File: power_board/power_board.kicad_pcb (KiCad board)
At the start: 2 copper layers, 62 parts, among them J1 Conn_01x02_Female, J10 Conn_01x01_Male, J11 Conn_01x01_Male, J12 Conn_01x01_Male, J13 Conn_01x04_Female, J2 Conn_01x02_Female, J3 Conn_01x02_Female, J4 Conn_01x02_Female, J5 Conn_01x02_Female, J6 Conn_01x01_Male, J7 Conn_01x01_Male, J8 Screw_Terminal_01x02, J9 Conn_01x01_Male, Q1 2N3904, Q2 2N3906, Q3 2N3904, SW1 SW_Push, U1 ACS758xCB-050B-PFF, U2 ACS758xCB-050B-PFF, U3 MCP2515-EST, U4 MAX31855KASA, U5 MCP2551-I-SN, U6 LM5166X, U7 ATmega328P-AU, Y1 16Mhz, Y2 16Mhz

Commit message: finishing touches
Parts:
- removed C11, C12: 560pF, Capacitor_SMD:C_0603_1608Metric
- removed C6: 10nF, Capacitor_SMD:C_0603_1608Metric
- removed L1, L2: 470ohm, Inductor_SMD:L_0603_1608Metric
- removed R10, R11: 100, Resistor_SMD:R_0603_1608Metric
- removed R6: 4.7k, Resistor_SMD:R_0603_1608Metric
- added J14: M7, TerminalBlock:TerminalBlock_bornier-2_P5.08mm, F.Cu at (81.7, 99.3)
- added J15: FAN, TerminalBlock:TerminalBlock_bornier-2_P5.08mm, F.Cu at (81.7, 107.3)
- added Q4: Q_NMOS_DGS, Package_TO_SOT_SMD:TO-263-2, F.Cu at (70.6, 100.9)
- J1: value Conn_01x02_Female -> PROG; footprint Connector_JST:JST_GH_BM02B-GHS-TBT_1x02-1MP_P1.25mm_Vertical -> Connector_PinHeader_2.54mm:PinHeader_1x05_P2.54mm_Vertical
- J10: value Conn_01x01_Male -> M4; footprint Connector:Banana_Jack_1Pin -> TerminalBlock:TerminalBlock_bornier-2_P5.08mm
- J11: value Conn_01x01_Male -> MainBoard; footprint Connector:Banana_Jack_1Pin -> TerminalBlock:TerminalBlock_bornier-2_P5.08mm
- J12: value Conn_01x01_Male -> M5; footprint Connector:Banana_Jack_1Pin -> TerminalBlock:TerminalBlock_bornier-2_P5.08mm
- J13: value Conn_01x04_Female -> M6; footprint Connector_PinHeader_2.54mm:PinHeader_1x04_P2.54mm_Horizontal -> TerminalBlock:TerminalBlock_bornier-2_P5.08mm
- J2: value Conn_01x02_Female -> M1; footprint Connector_JST:JST_GH_BM02B-GHS-TBT_1x02-1MP_P1.25mm_Vertical -> TerminalBlock:TerminalBlock_bornier-2_P5.08mm
- J3: value Conn_01x02_Female -> M2; footprint Connector_JST:JST_GH_BM02B-GHS-TBT_1x02-1MP_P1.25mm_Vertical -> TerminalBlock:TerminalBlock_bornier-2_P5.08mm
- J9: value Conn_01x01_Male -> M3; footprint Connector:Banana_Jack_1Pin -> TerminalBlock:TerminalBlock_bornier-2_P5.08mm
- Q1, Q3: value 2N3904 -> Q_NMOS_DGS; footprint Package_TO_SOT_SMD:SOT-23 -> Package_TO_SOT_SMD:TO-263-2
- Q2: value 2N3906 -> Q_NMOS_DGS; footprint Package_TO_SOT_SMD:SOT-23 -> Package_TO_SOT_SMD:TO-263-2
- R12: value R_US -> 0
- R2: value 1k -> 10k
- R3: value 27k -> 10k
- R4: value 4.7k -> 10k
- R5: value 1k -> 1.1k
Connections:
- net SYSTEM_SHUTOFF renamed Net-(U7-Pad11)
- J1 pad 1: GNDREF -> +5V
- J1 pad 2: PROBE -> RESET
- J10 pad 1: GNDREF -> +12V
- J11 pad 1: +12VA -> +5V
- J12 pad 1: GNDREF -> +12VA
- J13 pad 1: +5V -> +12VA
- J13 pad 2: TX -> GNDREF
- J2 pad 1: GNDREF -> +12V
- J2 pad 2: PROBE -> GNDREF
- J3 pad 1: GNDREF -> +12V
- J3 pad 2: PROBE -> GNDREF
- J4 pad 2: PROBE -> LEAK_DETECTED
- J5 pad 2: PROBE -> LEAK_DETECTED
- Q1 pad 1: GNDREF -> Net-(Q1-Pad1)
- Q1 pad 2: Net-(Q1-Pad2) -> LEAK_DETECTED
- Q1 pad 3: Net-(Q1-Pad3) -> GNDREF
- Q2 pad 1: +5V -> Net-(Q2-Pad1)
- Q2 pad 2: Net-(Q2-Pad2) -> LEAK_DETECTED
- Q2 pad 3: LEAK_DETECTED -> GNDREF
- Q3 pad 1: GNDREF -> Net-(Q1-Pad1)
- Q3 pad 2: Net-(Q3-Pad2) -> LEAK_DETECTED
- Q3 pad 3: Net-(Q1-Pad3) -> GNDREF
- R14 pad 1: RESET -> +5V
- R14 pad 2: +5V -> RESET
- R2 pad 1: Net-(Q2-Pad2) -> +5VA
- R2 pad 2: PROBE -> LEAK_DETECTED
- R3 pad 1: Net-(Q2-Pad2) -> +5VA
- R3 pad 2: +5V -> LEAK_DETECTED
- R4 pad 1: LEAK_DETECTED -> +5VA
- R4 pad 2: Net-(Q1-Pad2) -> +48V
- R5 pad 2: LEAK_DETECTED -> +5VA
- REG1 pad 2: Net-(Q1-Pad3) -> Net-(Q2-Pad1)
- REG1 pad 3: GNDREF -> Net-(Q2-Pad1)
- REG2 pad 2: Net-(Q1-Pad3) -> Net-(Q1-Pad1)
- REG2 pad 3: GNDREF -> Net-(Q1-Pad1)
- U3 pad 11: Net-(U3-Pad11) -> RX1BF
- U3 pad 12: Net-(U3-Pad12) -> RX_INT
- U3 pad 4: Net-(U3-Pad4) -> TX0RTS
- U3 pad 5: Net-(U3-Pad5) -> TX1RTS
- U3 pad 7: Net-(U3-Pad7) -> TX2RTS
- U4 pad 2: Net-(C6-Pad2) -> Net-(J8-Pad2)
- U4 pad 3: Net-(C6-Pad1) -> Net-(J8-Pad1)
- U7 pad 1: Net-(U7-Pad1) -> RX_INT
- U7 pad 25: Net-(U7-Pad25) -> RX1BF
- U7 pad 26: Net-(U7-Pad26) -> TX0RTS
- U7 pad 27: Net-(U7-Pad27) -> TX1RTS
- U7 pad 28: Net-(U7-Pad28) -> TX2RTS

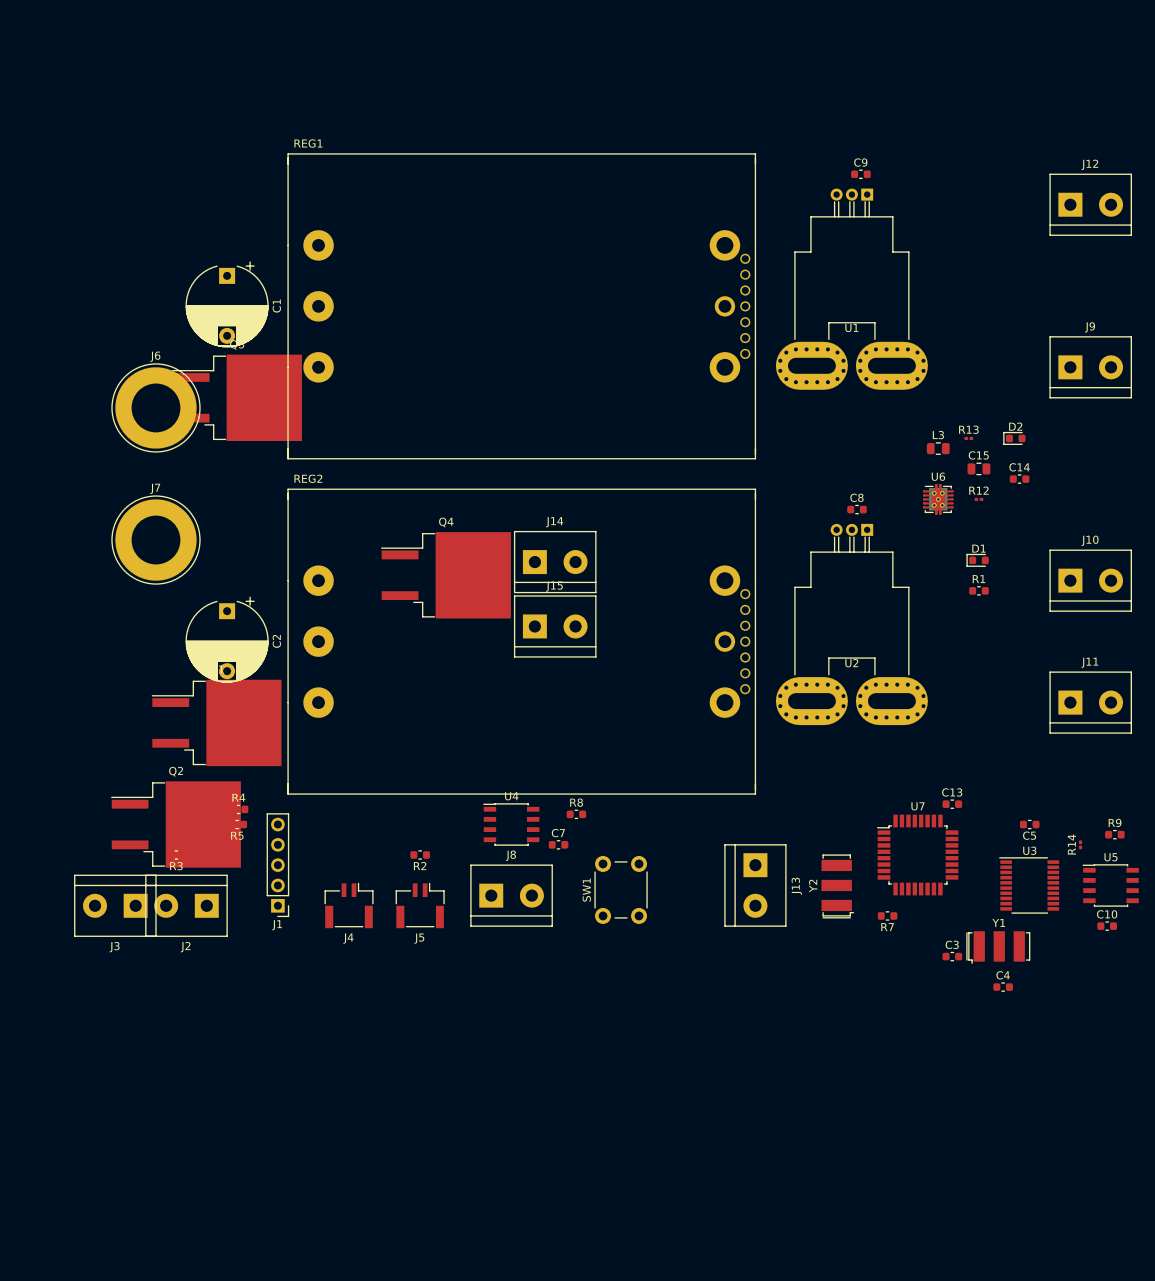
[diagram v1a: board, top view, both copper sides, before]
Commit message: Finished adding power regulator isolation
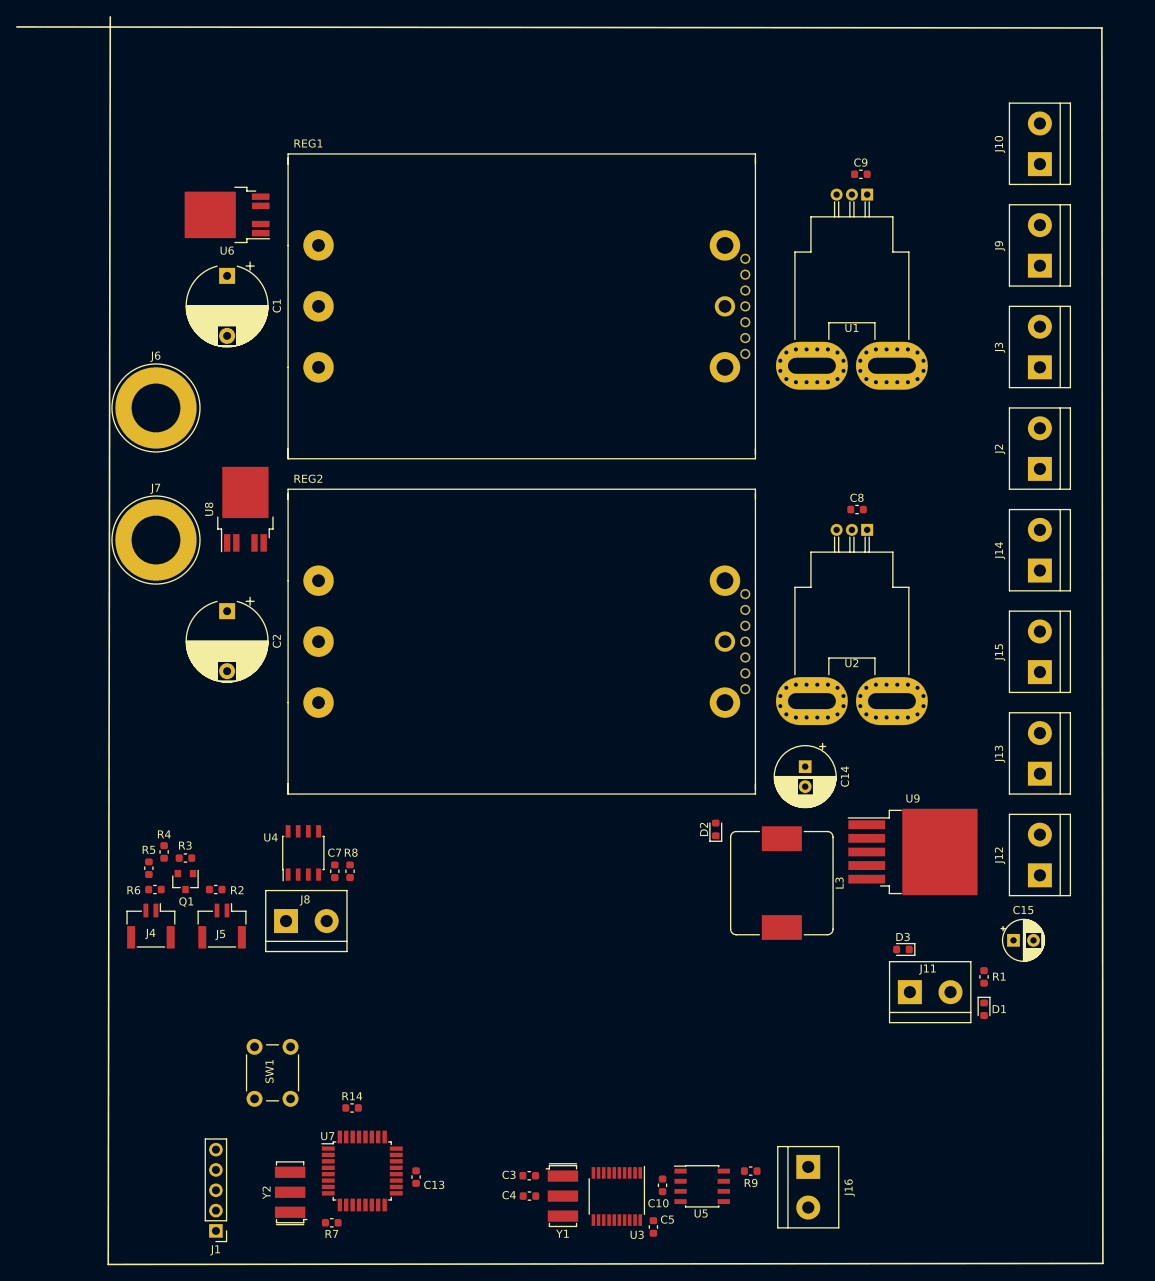
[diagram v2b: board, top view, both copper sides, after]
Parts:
- removed Q2, Q3, Q4: Q_NMOS_DGS, Package_TO_SOT_SMD:TO-263-2
- removed R12: 0, Resistor_SMD:R_0201_0603Metric
- removed R13: 0.5, Resistor_SMD:R_0201_0603Metric
- added D3: --, Diode_SMD:D_0603_1608Metric, F.Cu at (127.7, 147.7)
- added J16: Screw_Terminal_01x02, TerminalBlock:TerminalBlock_bornier-2_P5.08mm, F.Cu at (115.8, 174.9)
- added R6: 10k, Resistor_SMD:R_0603_1608Metric, F.Cu at (34.2, 140.2)
- added U8: BTS6163D, Package_TO_SOT_SMD:TO-252-4, F.Cu at (45.5, 92.7)
- added U9: LM2596S-5, Package_TO_SOT_SMD:TO-263-5_TabPin3, F.Cu at (128.9, 135.5)
- C1, C2: value CP -> 300uF
- C14: value 2.2uF -> 680uF; footprint Capacitor_SMD:C_0603_1608Metric -> Capacitor_THT:CP_Radial_D7.5mm_P2.50mm
- C15: value 47uF -> 220uF; footprint Capacitor_SMD:C_0805_2012Metric -> Capacitor_THT:CP_Radial_D5.0mm_P2.50mm
- D2: value D_Schottky -> 1N5824
- L3: value 150uH -> 33uH; footprint Inductor_SMD:L_0805_2012Metric -> Inductor_SMD:L_Bourns_SRP1245A
- Q1: value Q_NMOS_DGS -> 2N3906; footprint Package_TO_SOT_SMD:TO-263-2 -> Package_TO_SOT_SMD:SOT-23
- R14: footprint Resistor_SMD:R_0201_0603Metric -> Resistor_SMD:R_0603_1608Metric
- R2: value 10k -> 1k
- U6: value LM5166X -> BTS6163D; footprint Package_SON:Texas_S-PVSON-N10_ThermalVias -> Package_TO_SOT_SMD:TO-252-4
- moved J3 131.6 mm to (144.8, 74.9), turned to 90 degrees
- moved J2 117.6 mm to (144.8, 87.6), turned to 90 degrees
- moved R14 96.8 mm to (58.8, 167.5), turned to 0 degrees
- moved U6 95.7 mm to (43.2, 55.9), turned to 180 degrees
- moved J12 83.9 mm to (144.8, 138.4), turned to 90 degrees
- moved C13 81.6 mm to (66.8, 176.1), turned to 90 degrees
- moved U7 79.9 mm to (60.1, 175.4)
- moved R7 79.4 mm to (56.3, 181.9)
- moved Y2 78.4 mm to (51.1, 178.1)
- moved C5 68.9 mm to (96.5, 182.4), turned to 270 degrees
- moved C4 64.7 mm to (81.0, 178.5), turned to 180 degrees
- moved U3 64.6 mm to (91.9, 178.6), turned to 270 degrees
- moved C10 64.3 mm to (97.6, 177.2), turned to 90 degrees
- moved U5 63.5 mm to (102.6, 177.3)
- moved J15 63.4 mm to (144.8, 113.0), turned to 90 degrees
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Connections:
- C1 pad 1: +48V -> Net-(C1-Pad1)
- C2 pad 1: +48V -> Net-(C2-Pad1)
- D2 pad 1: +5V -> Net-(D2-Pad1)
- D2 pad 2: Net-(D2-Pad2) -> GNDREF
- J4 pad 2: LEAK_DETECTED -> Net-(J4-Pad2)
- J5 pad 2: LEAK_DETECTED -> Net-(J4-Pad2)
- L3 pad 1: Net-(L3-Pad1) -> Net-(D2-Pad1)
- L3 pad 2: Net-(D2-Pad2) -> Net-(C15-Pad1)
- Q1 pad 2: LEAK_DETECTED -> +5VA
- Q1 pad 3: GNDREF -> SHUTOFF
- R2 pad 1: +5VA -> Net-(J4-Pad2)
- R2 pad 2: LEAK_DETECTED -> Net-(Q1-Pad1)
- R3 pad 1: +5VA -> Net-(Q1-Pad1)
- R3 pad 2: LEAK_DETECTED -> +5VA
- REG1 pad 1: +48V -> Net-(C1-Pad1)
- REG1 pad 2: Net-(Q2-Pad1) -> GNDREF
- REG1 pad 3: Net-(Q2-Pad1) -> GNDREF
- REG2 pad 1: +48V -> Net-(C2-Pad1)
- REG2 pad 2: Net-(Q1-Pad1) -> GNDREF
- REG2 pad 3: Net-(Q1-Pad1) -> GNDREF
- U4 pad 2: Net-(J8-Pad2) -> Net-(J8-Pad1)
- U4 pad 3: Net-(J8-Pad1) -> Net-(J8-Pad2)
- U6 pad 1: Net-(L3-Pad1) -> Net-(C1-Pad1)
- U6 pad 2: +12VA -> SHUTOFF
- U6 pad 3: GNDREF -> +48V
- U6 pad 5: Net-(R12-Pad1) -> Net-(C1-Pad1)

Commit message: PCB Layout work
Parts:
- added J17: MB_interface, Connector_PinHeader_2.54mm:PinHeader_1x04_P2.54mm_Vertical, F.Cu at (194.3, 130.2)
- added J19: 12V_1, TerminalBlock:TerminalBlock_bornier-2_P5.08mm, F.Cu at (219.1, 41.9)
- added J20: 12V_2, TerminalBlock:TerminalBlock_bornier-2_P5.08mm, F.Cu at (182.9, 41.9)
- added J21: 12V_3, TerminalBlock:TerminalBlock_bornier-2_P5.08mm, F.Cu at (207.0, 41.9)
- added J22: 12V_4, TerminalBlock:TerminalBlock_bornier-2_P5.08mm, F.Cu at (194.9, 41.9)
- added J23: 48V_1, TerminalBlock:TerminalBlock_bornier-2_P5.08mm, F.Cu at (221.6, 148.0)
- added J24: 48V_2, TerminalBlock:TerminalBlock_bornier-2_P5.08mm, F.Cu at (221.6, 111.8)
- added J25: 48V_3, TerminalBlock:TerminalBlock_bornier-2_P5.08mm, F.Cu at (221.6, 135.9)
- added J26: 48V_4, TerminalBlock:TerminalBlock_bornier-2_P5.08mm, F.Cu at (221.6, 123.8)
- C1, C2, REG1, REG2, U1, U2, U6, U8: moved to B.Cu
- J11: value MainBoard -> 5V_1
- Y1: value 16Mhz -> 20Mhz
- moved SW1 201.6 mm to (223.6, 69.8), turned to 270 degrees
- moved J8 180.0 mm to (221.5, 87.6), turned to 90 degrees
- moved R7 164.0 mm to (198.1, 99.6), turned to 270 degrees
- moved J1 161.3 mm to (180.3, 100.3)
- moved C7 161.0 mm to (210.8, 91.6), turned to 180 degrees
- moved U4 160.9 mm to (208.5, 95.6), turned to 180 degrees
- moved Y2 160.9 mm to (194.3, 104.8), turned to 180 degrees
- moved R8 159.7 mm to (210.8, 89.7), turned to 180 degrees
- moved J4 157.9 mm to (191.5, 147.1)
- moved R2 157.9 mm to (199.6, 142.6)
- moved J5 157.9 mm to (200.4, 147.1)
- moved Q1 157.9 mm to (195.8, 141.6)
- moved R3 157.9 mm to (195.8, 138.6)
- moved R4 157.9 mm to (193.2, 137.9)
- moved R5 157.9 mm to (191.3, 139.9)
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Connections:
- net Net-(C2-Pad1) renamed 48V
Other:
- board outline added: 165.3 x 121.3 mm

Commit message: HIgh power routing work
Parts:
- C1, C2: moved to F.Cu
- U6, U8: value BTS6163D -> BTS50085-1TMA; footprint Package_TO_SOT_SMD:TO-252-4 -> Package_TO_SOT_SMD:Infineon_PG-TO-220-7Lead_TabPin8
- moved C2 103.9 mm to (48.5, 140.2)
- moved C1 60.2 mm to (52.3, 126.9)
- moved J6 8.25 mm to (81.3, 104.1)
- moved REG1 2.09 mm to (103.4, 129.7)
- moved U1 2.09 mm to (125.4, 60.7)
- moved C8 2.09 mm to (127.5, 61.5)
- moved REG2 2.03 mm to (144.9, 129.7)
- moved U2 2.03 mm to (166.8, 60.6)
- moved C9 2.03 mm to (168.9, 61.5)
- moved U6 1.49 mm to (118.6, 142.7)
- moved U8 1.21 mm to (160.1, 142.7)
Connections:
- U6 pad 2: SHUTOFF -> Net-(C1-Pad1)
- U6 pad 3: +48V -> SHUTOFF
- U6 pad 4: Net-(U6-Pad4) -> +48V
- U6 pad 5: Net-(C1-Pad1) -> Net-(U6-Pad5)
- U8 pad 2: SHUTOFF -> 48V
- U8 pad 3: +48V -> SHUTOFF
- U8 pad 4: Net-(U8-Pad4) -> +48V
- U8 pad 5: 48V -> Net-(U8-Pad5)
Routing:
- net SHUTOFF: track 0.00 -> 82.2 mm
- net Net-(C1-Pad1): vias 0 -> 8
- net 48V: vias 0 -> 8
- net +48V: vias 0 -> 109
- added copper zone on B.Cu, net +48V
- added copper zone on F.Cu, net +48V
- added copper zone on B.Cu, net 48V
- added copper zone on F.Cu, net 48V
- added copper zone on B.Cu, net Net-(C1-Pad1)
- added copper zone on F.Cu, net Net-(C1-Pad1)
